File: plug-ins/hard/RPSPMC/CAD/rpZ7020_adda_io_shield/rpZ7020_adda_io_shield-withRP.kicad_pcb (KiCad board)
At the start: 4 copper layers, 70.6 x 94.5 mm, 41 parts, among them J1 Samtec_ASP-134486-01, J2 Conn_01x03_Socket, J2-FMC-RP1 Conn_02x20, J2-PWR3 Conn_01x03_Pin, J3-FMC-POWER1 Conn_02x06_Odd_Even, J3-PWR12 Conn_01x02_Pin, J4-FMC-AUX1 Conn_02x06_Odd_Even

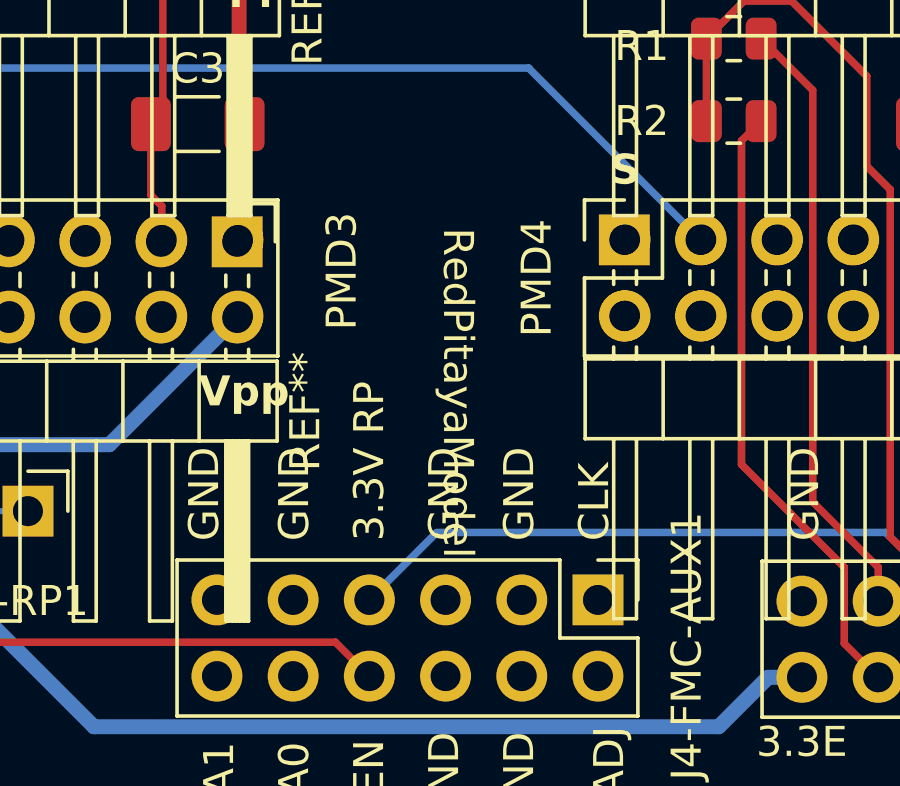
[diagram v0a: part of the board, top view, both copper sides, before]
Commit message: updated 3d model
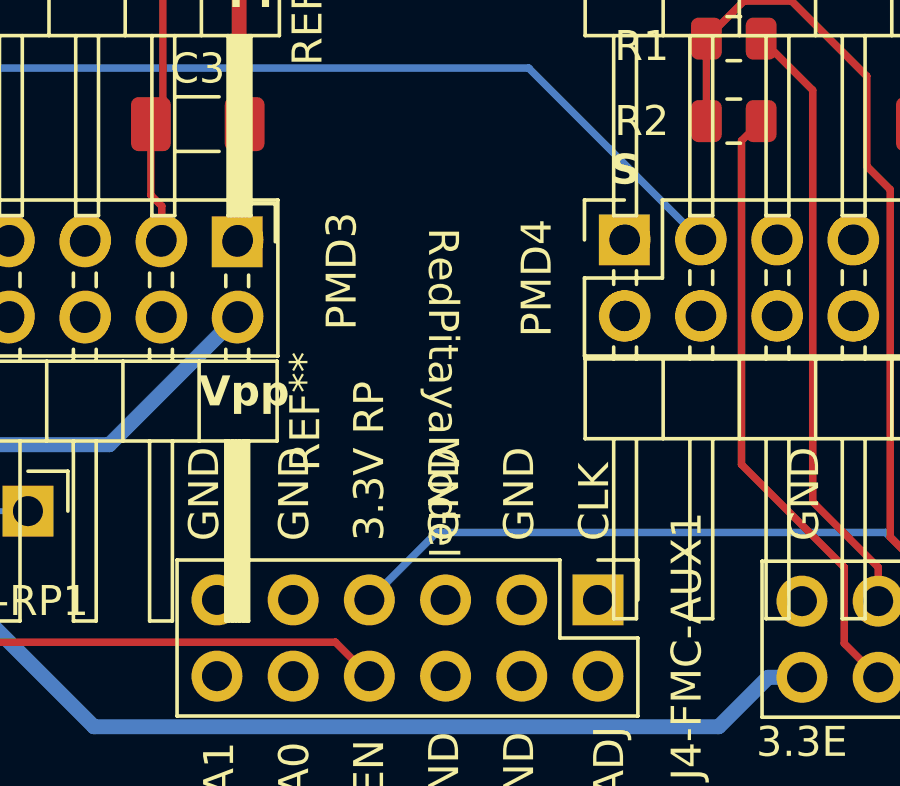
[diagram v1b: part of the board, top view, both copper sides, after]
